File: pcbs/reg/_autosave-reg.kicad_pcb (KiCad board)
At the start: 2 copper layers, 21 parts, among them J1 Conn_01x01_Female, J10 Conn_01x08, J11 Conn_01x08, J2 Conn_01x02_Male, J3 Conn_Coaxial, J4 Conn_01x08, J5 Conn_01x08, J6 Conn_01x08, J7 Conn_01x08, J8 Conn_01x08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

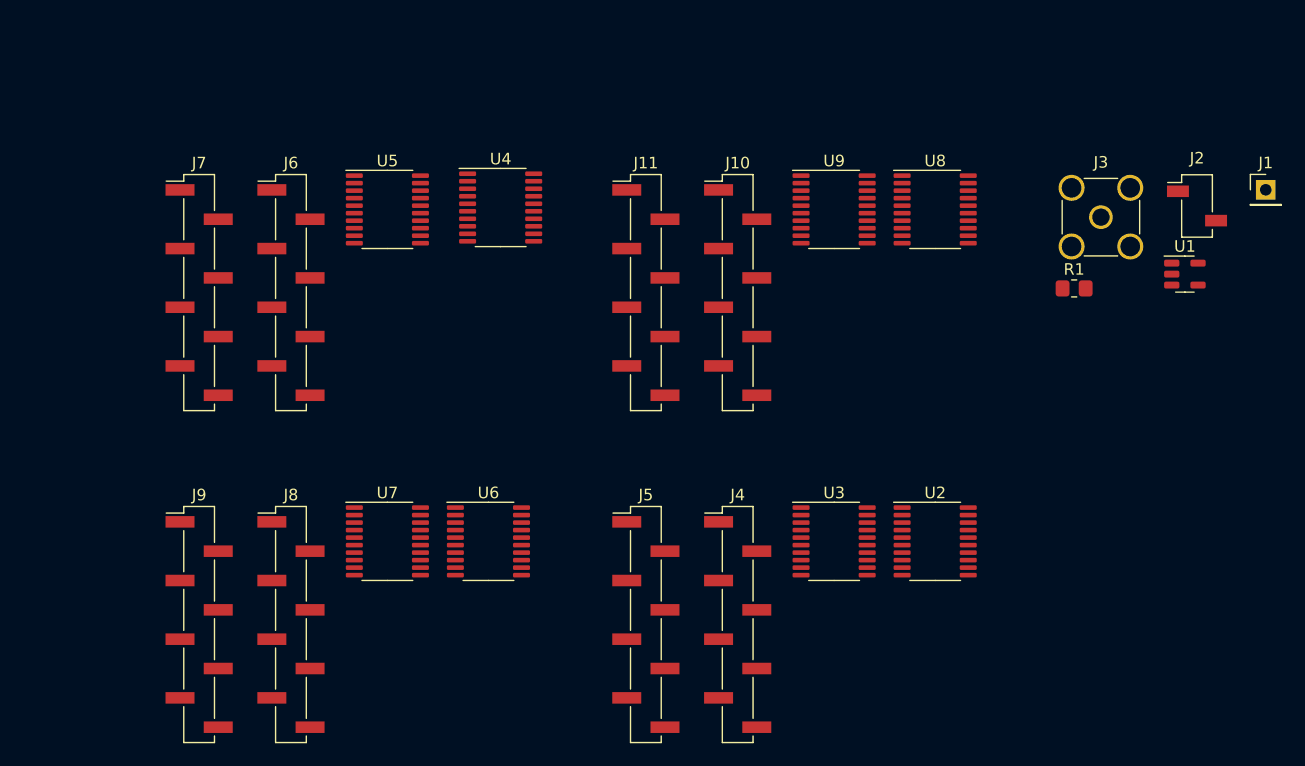
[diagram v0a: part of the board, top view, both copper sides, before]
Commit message: v1 8view borads
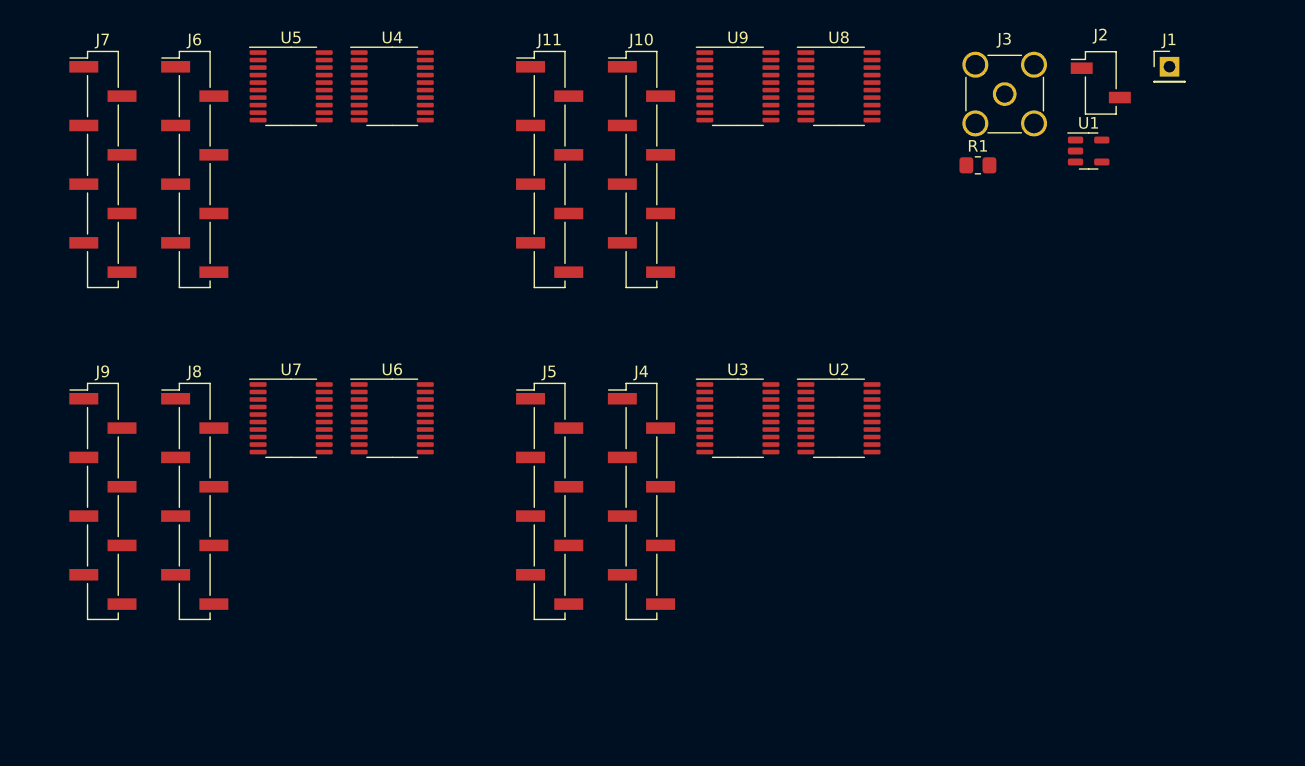
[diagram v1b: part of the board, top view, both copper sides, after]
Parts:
- moved U4 14.1 mm to (191.5, 38.3)
- moved J10 13.5 mm to (213.1, 45.5)
- moved J4 13.5 mm to (213.1, 74.2)
- moved J6 13.5 mm to (174.4, 45.5)
- moved J8 13.5 mm to (174.4, 74.2)
- moved R1 13.5 mm to (242.2, 45.1)
- moved U2 13.5 mm to (230.2, 67.0)
- moved U3 13.5 mm to (221.5, 67.0)
- moved U8 13.5 mm to (230.2, 38.3)
- moved U9 13.5 mm to (221.5, 38.3)
- moved J11 13.5 mm to (205.2, 45.5)
- moved J2 13.5 mm to (252.9, 38.0)
- moved J3 13.5 mm to (244.6, 38.9)
- moved J5 13.5 mm to (205.2, 74.2)
- moved J7 13.5 mm to (166.5, 45.5)
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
